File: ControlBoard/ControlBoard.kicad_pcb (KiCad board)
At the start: 2 copper layers, 144 x 106 mm, 187 parts, among them J1 PowerIn, J10 Conn_01x01, J11 Conn_01x01, J12 Conn_01x01, J13 Conn_01x01, J14 Conn_01x01, J15 Conn_01x01, J16 Conn_01x06, J17 Conn_01x06, J18 Conn_01x06, J19 HALLSENS, J2 UART, J20 Conn_01x06, J21 HALLSENS2, J22 PowerIn, J3 ICSP, J4 MTR1, J5 MTR2, J6 Ultrasonic Transmitter, J7 Ultrasonic Receiver, J8 Conn_01x01, J9 Conn_01x01, Q1 2N3904, Q2 2N3904, SW1 SW_Push, U1 LM358, U10 LMT85, U11 74HC138, U12 4051, U13 4051, U14 74HC14, U2 LM358, U3 LM358, U4 LM358, U5 ATMEGA328P-PU, U6 LM7805_TO220, U7 74HC595, U8 L298D, U9 74HC595, Y1 16MHz

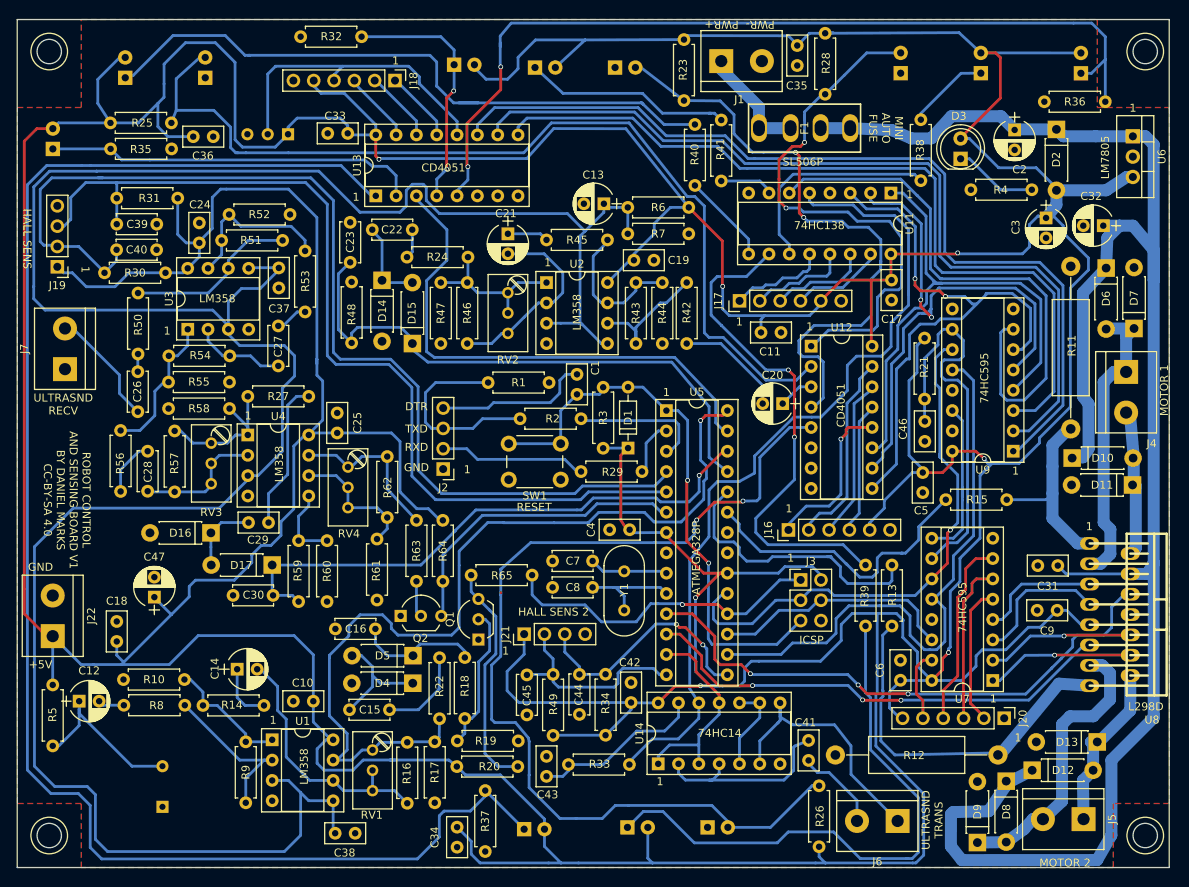
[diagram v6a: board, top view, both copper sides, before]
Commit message: Begin code for controlling robot with command line
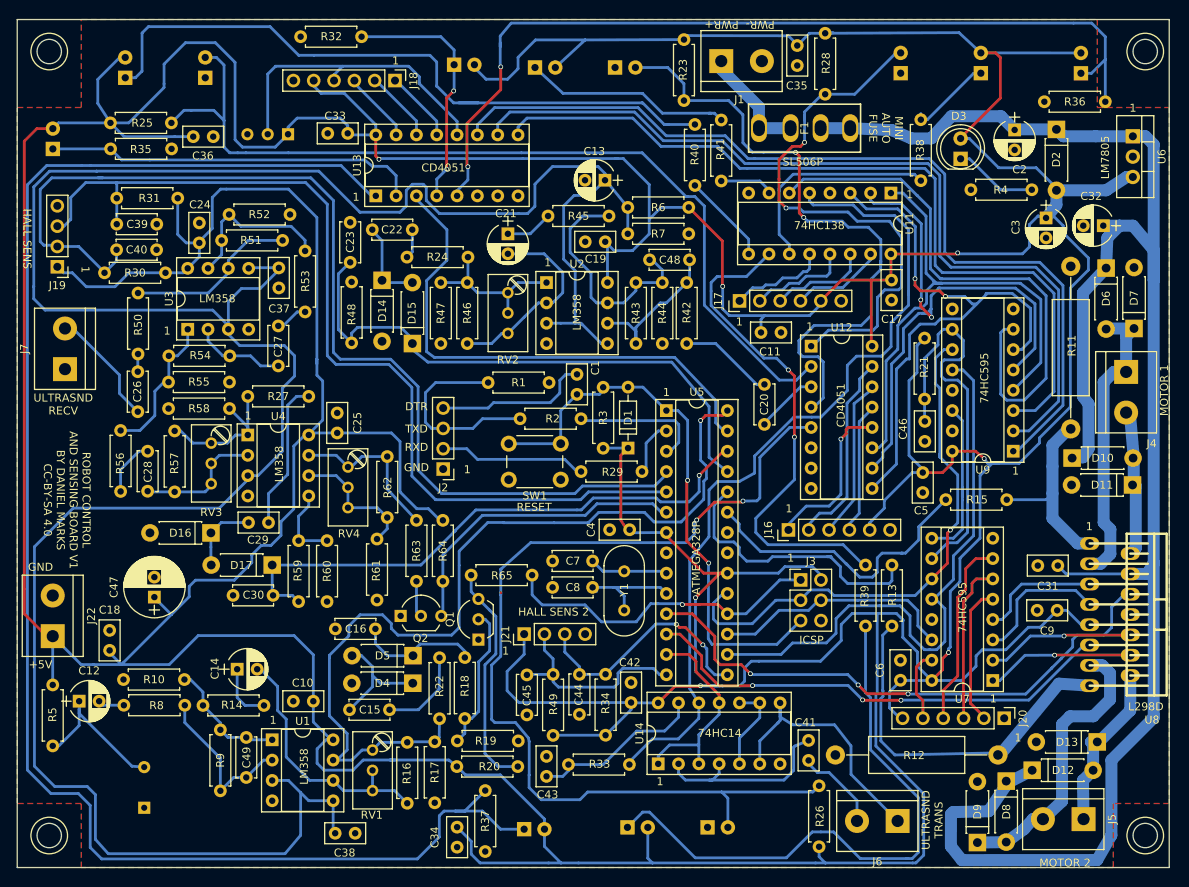
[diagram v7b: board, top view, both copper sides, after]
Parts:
- added C48: 470 pF, Capacitors_THT:C_Disc_D5.0mm_W2.5mm_P5.00mm, F.Cu at (134.0, 69.0)
- added C49: 100 pF, Capacitors_THT:C_Disc_D5.0mm_W2.5mm_P5.00mm, F.Cu at (83.6, 128.7)
- C20: value 1 uF -> 100 nF; footprint Capacitors_THT:CP_Radial_D5.0mm_P2.50mm -> Capacitors_THT:C_Disc_D5.0mm_W2.5mm_P5.00mm
- C23: value 1000 pF -> 10 nF
- C38: value 100 nF -> 220 nF
- C47: value 100 uF -> 1000 uF; footprint Capacitors_THT:CP_Radial_D5.0mm_P2.50mm -> Capacitors_THT:CP_Radial_D7.5mm_P2.50mm
- R33: value 10k -> 100k
- R48: value 10k -> 1M
- moved C19 4.26 mm to (128.5, 66.8), turned to 180 degrees
- moved R9 3.51 mm to (80.4, 135.4)
- moved C20 3.31 mm to (148.4, 84.6), turned to 270 degrees
- moved R45 2.99 mm to (129.0, 63.6)
- moved C13 2.94 mm to (128.5, 59.1)
- moved MK1 2.28 mm to (70.9, 135.0)
- moved C18 1.43 mm to (66.5, 117.9)
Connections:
- R42 pad 1: Net-(C20-Pad2) -> Net-(C20-Pad1)
- U12 pad 3: Net-(C20-Pad1) -> Net-(C20-Pad2)
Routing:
- net 2V5: track 311.5 -> 326.2 mm
- net Net-(C48-Pad1): track 18.3 -> 30.7 mm
- net Net-(C20-Pad1): track 4.43 -> 11.8 mm
- net Net-(C20-Pad2): track 13.9 -> 7.90 mm
- net Net-(PT3-Pad2): track 118.9 -> 114.9 mm
- net Net-(ID3-Pad1): track 82.9 -> 86.8 mm
- net Net-(C48-Pad2): track 16.2 -> 19.2 mm
- net Net-(PT4-Pad2): track 77.0 -> 79.9 mm
- net Net-(PDT1-Pad1): track 196.7 -> 199.0 mm
- net Net-(C12-Pad1): track 21.1 -> 18.8 mm
- net Net-(ID2-Pad1): track 72.3 -> 73.8 mm
- net +5V: track 1088.6 -> 1089.6 mm
- net Net-(PT2-Pad2): track 124.1 -> 125.0 mm
- net Net-(C21-Pad1): track 5.14 -> 5.94 mm
- net Net-(R39-Pad2): track 63.3 -> 62.6 mm

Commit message: Added some filter capacitors
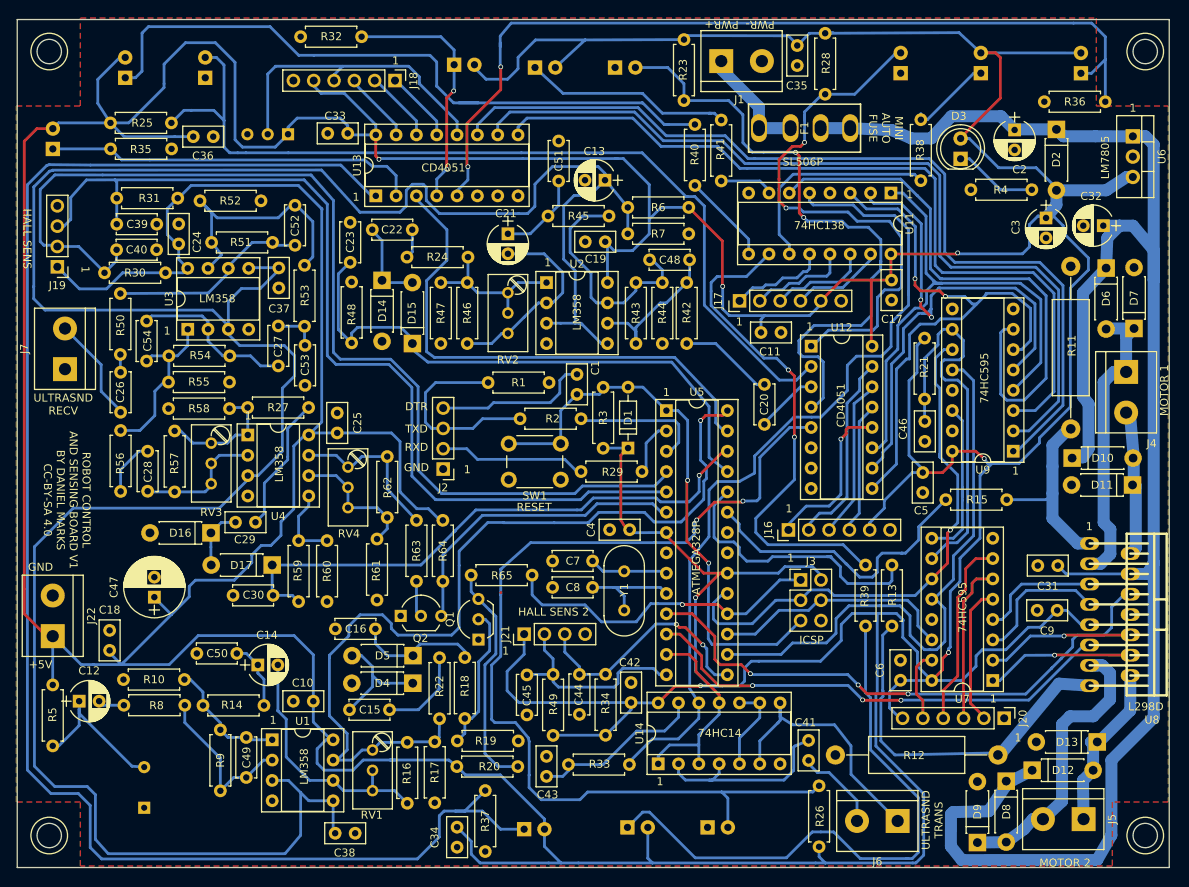
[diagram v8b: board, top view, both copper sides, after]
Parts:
- added C50: 100 nF, Capacitors_THT:C_Disc_D5.0mm_W2.5mm_P5.00mm, F.Cu at (77.5, 118.2)
- added C51: 100 nF, Capacitors_THT:C_Disc_D5.0mm_W2.5mm_P5.00mm, F.Cu at (122.7, 59.2)
- added C52: 68 pF, Capacitors_THT:C_Disc_D5.0mm_W2.5mm_P5.00mm, F.Cu at (89.7, 62.2)
- added C53: 10 nF, Capacitors_THT:C_Disc_D5.0mm_W2.5mm_P5.00mm, F.Cu at (91.0, 84.7)
- added C54: 68 pF, Capacitors_THT:C_Disc_D5.0mm_W2.5mm_P5.00mm, F.Cu at (71.2, 81.7)
- moved R52 4.01 mm to (85.5, 61.7)
- moved C14 2.64 mm to (85.1, 119.7)
- moved C24 2.58 mm to (75.2, 67.1)
- moved R50 2.21 mm to (67.9, 73.2)
- moved C26 2.15 mm to (67.9, 83.1)
- moved R53 1.79 mm to (90.9, 77.3)
- moved C29 1.63 mm to (84.8, 101.8)
- moved R27 1.39 mm to (83.8, 87.5)
- moved R51 1.28 mm to (79.3, 66.9)
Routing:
- net Net-(C52-Pad1): track 20.1 -> 32.8 mm
- net Net-(C27-Pad1): track 11.5 -> 20.7 mm
- net Net-(C21-Pad1): track 5.94 -> 10.9 mm
- net Net-(C52-Pad2): track 22.6 -> 25.9 mm
- net Net-(R27-Pad1): track 19.3 -> 15.9 mm
- net Net-(C54-Pad1): track 18.5 -> 21.5 mm
- net Net-(C27-Pad2): track 4.07 -> 6.32 mm
- net Net-(C29-Pad1): track 18.8 -> 17.1 mm
- net Net-(C29-Pad2): track 9.27 -> 7.64 mm
- net Net-(C14-Pad1): track 7.30 -> 8.60 mm
- net Net-(C39-Pad1): track 119.8 -> 120.4 mm
